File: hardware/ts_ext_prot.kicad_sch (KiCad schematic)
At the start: 4 parts

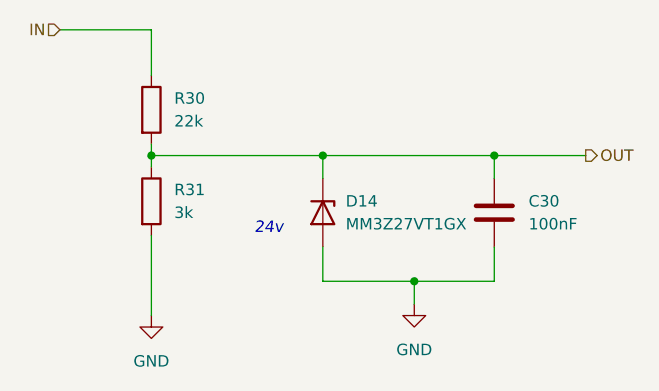
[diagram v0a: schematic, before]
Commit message: 0xERC State
Schematic needs only simulation and veryfying component choice for now
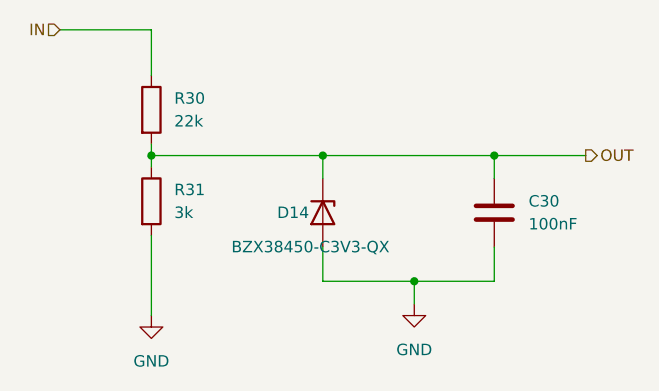
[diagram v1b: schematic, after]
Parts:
- D14: value MM3Z27VT1GX -> BZX38450-C3V3-QX; footprint Diode_SMD:D_SMB -> Diode_SMD:D_SOD-323_HandSoldering
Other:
- note removed: "24v"
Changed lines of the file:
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@@
     (stroke (width 0) (type default) (color 0 0 0 0))
-  )
-  (text "24v\n" (at 129.54 92.71 0)
-    (effects (font (size 1.27 1.27) italic) (justify left bottom))
   )
   (hierarchical_label "IN" (shape input) (at 107.95 69.85 180)
@@
   )
   (symbol (lib_id "Device:D_Zener") (at 137.16 90.17 270) (unit 1)
-    (in_bom yes) (on_board yes) (fields_autoplaced)
-    (property "Reference" "D14" (id 0) (at 139.7 88.8999 90)
+    (in_bom yes) (on_board yes)
+    (property "Reference" "D14" (id 0) (at 132.08 90.17 90)
       (effects (font (size 1.27 1.27)) (justify left))
     )
-    (property "Value" "MM3Z27VT1GX" (id 1) (at 139.7 91.4399 90)
+    (property "Value" "BZX38450-C3V3-QX" (id 1) (at 127 93.98 90)
       (effects (font (size 1.27 1.27)) (justify left))
     )
-    (property "Footprint" "Diode_SMD:D_SMB" (id 2) (at 137.16 90.17 0)
+    (property "Footprint" "Diode_SMD:D_SOD-323_HandSoldering" (id 2) (at 137.16 90.17 0)
       (effects (font (size 1.27 1.27)) hide)
     )
-    (property "Datasheet" "~" (id 3) (at 137.16 90.17 0)
+    (property "Datasheet" "https://www.mouser.pl/datasheet/2/916/BZX38450_Q_SER-2580608.pdf" (id 3) (at 137.16 90.17 0)
       (effects (font (size 1.27 1.27)) hide)
     )

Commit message: working simulations, assigned footprints
"nightly" relase
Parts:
- C30: value 100nF -> 10nF
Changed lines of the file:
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@@
       (effects (font (size 1.27 1.27)) (justify left))
     )
-    (property "Value" "100nF" (id 1) (at 160.02 91.4399 0)
+    (property "Value" "10nF" (id 1) (at 160.02 91.4399 0)
       (effects (font (size 1.27 1.27)) (justify left))
     )

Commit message: kończymy balet na dziś
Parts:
- R30, R31: footprint Resistor_SMD:R_0603_1608Metric -> Resistor_SMD:R_0603_1608Metric_Pad0.98x0.95mm_HandSolder
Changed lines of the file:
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@@
       (effects (font (size 1.27 1.27)) (justify left))
     )
-    (property "Footprint" "Resistor_SMD:R_0603_1608Metric" (id 2) (at 116.332 88.9 90)
+    (property "Footprint" "Resistor_SMD:R_0603_1608Metric_Pad0.98x0.95mm_HandSolder" (id 2) (at 116.332 88.9 90)
       (effects (font (size 1.27 1.27)) hide)
     )
@@
       (effects (font (size 1.27 1.27)) (justify left))
     )
-    (property "Footprint" "Resistor_SMD:R_0603_1608Metric" (id 2) (at 116.332 78.74 90)
+    (property "Footprint" "Resistor_SMD:R_0603_1608Metric_Pad0.98x0.95mm_HandSolder" (id 2) (at 116.332 78.74 90)
       (effects (font (size 1.27 1.27)) hide)
     )

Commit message: kurde no jeszcze nie skonczylem ale sune dalej
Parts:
- C30: footprint Capacitor_SMD:C_0201_0603Metric_Pad0.64x0.40mm_HandSolder -> Capacitor_SMD:C_0603_1608Metric_Pad1.08x0.95mm_HandSolder
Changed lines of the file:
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@@
       (effects (font (size 1.27 1.27)) (justify left))
     )
-    (property "Footprint" "Capacitor_SMD:C_0201_0603Metric_Pad0.64x0.40mm_HandSolder" (id 2) (at 157.1752 93.98 0)
+    (property "Footprint" "Capacitor_SMD:C_0603_1608Metric_Pad1.08x0.95mm_HandSolder" (id 2) (at 157.1752 93.98 0)
       (effects (font (size 1.27 1.27)) hide)
     )

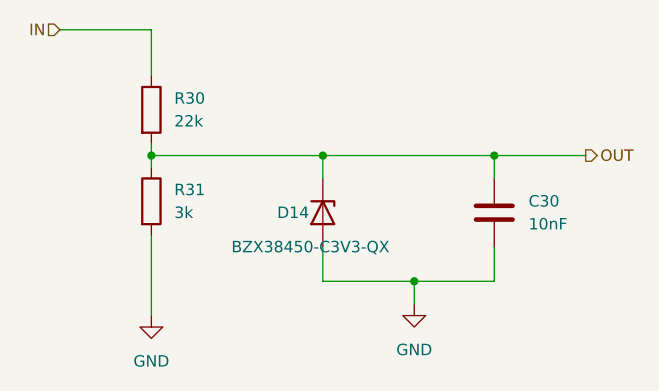
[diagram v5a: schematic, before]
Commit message: Schematic redesign for 23 rules, new pressure buffer, protection fix
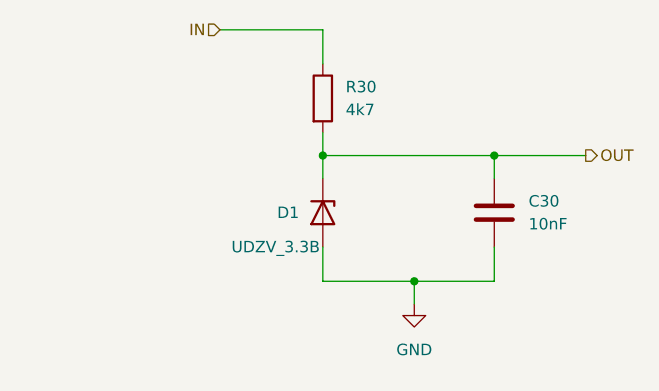
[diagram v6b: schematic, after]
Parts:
- removed D14: BZX38450-C3V3-QX, Diode_SMD:D_SOD-323_HandSoldering, symbol Device:D_Zener
- removed R31: 3k, Resistor_SMD:R_0603_1608Metric_Pad0.98x0.95mm_HandSolder, symbol Device:R
- added D1: UDZV_3.3B, Diode_SMD:D_SOD-323_HandSoldering, symbol Device:D_Zener
- R30: value 22k -> 4k7
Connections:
- net GND: now also D1.2 (A)
- net OUT: now also D1.1 (K)
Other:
- moved on the sheet: R30
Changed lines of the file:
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@@
   (junction (at 156.21 83.82) (diameter 0) (color 0 0 0 0)
-  )
-  (junction (at 118.11 83.82) (diameter 0) (color 0 0 0 0)
   )
   (junction (at 137.16 83.82) (diameter 0) (color 0 0 0 0)
@@
   (junction (at 147.32 97.79) (diameter 0) (color 0 0 0 0)
   )
-  (wire (pts (xy 107.95 69.85) (xy 118.11 69.85))
+  (wire (pts (xy 125.73 69.85) (xy 137.16 69.85))
     (stroke (width 0) (type default))
   )
-  (wire (pts (xy 118.11 82.55) (xy 118.11 83.82))
+  (wire (pts (xy 137.16 81.28) (xy 137.16 83.82))
     (stroke (width 0) (type default))
   )
   (wire (pts (xy 137.16 97.79) (xy 137.16 93.98))
-    (stroke (width 0) (type default))
-  )
-  (wire (pts (xy 118.11 83.82) (xy 118.11 85.09))
     (stroke (width 0) (type default))
   )
@@
     (stroke (width 0) (type default))
   )
-  (wire (pts (xy 118.11 74.93) (xy 118.11 69.85))
+  (wire (pts (xy 137.16 73.66) (xy 137.16 69.85))
     (stroke (width 0) (type default))
   )
@@
     (stroke (width 0) (type default))
   )
-  (wire (pts (xy 118.11 83.82) (xy 137.16 83.82))
-    (stroke (width 0) (type default))
-  )
-  (wire (pts (xy 118.11 92.71) (xy 118.11 101.6))
-    (stroke (width 0) (type default))
-  )
   (wire (pts (xy 147.32 100.33) (xy 147.32 97.79))
     (stroke (width 0) (type default))
@@
     (stroke (width 0) (type default))
   )
-  (hierarchical_label "IN" (shape input) (at 107.95 69.85 180) (fields_autoplaced)
+  (hierarchical_label "IN" (shape input) (at 125.73 69.85 180) (fields_autoplaced)
     (effects (font (size 1.27 1.27)) (justify right))
   )
@@
     (effects (font (size 1.27 1.27)) (justify left))
   )
-  (symbol (lib_id "Device:R") (at 118.11 88.9 0) (unit 1)
-    (in_bom yes) (on_board yes) (dnp no) (fields_autoplaced)
-    (property "Reference" "R31" (at 120.65 87.6299 0)
+  (symbol (lib_id "Device:D_Zener") (at 137.16 90.17 270) (unit 1)
+    (in_bom yes) (on_board yes) (dnp no)
+    (property "Reference" "D1" (at 132.08 90.17 90)
       (effects (font (size 1.27 1.27)) (justify left))
     )
-    (property "Value" "3k" (at 120.65 90.1699 0)
+    (property "Value" "UDZV_3.3B" (at 127 93.98 90)
       (effects (font (size 1.27 1.27)) (justify left))
     )
-    (property "Footprint" "Resistor_SMD:R_0603_1608Metric_Pad0.98x0.95mm_HandSolder" (at 116.332 88.9 90)
+    (property "Footprint" "Diode_SMD:D_SOD-323_HandSoldering" (at 137.16 90.17 0)
       (effects (font (size 1.27 1.27)) hide)
     )
-    (property "Datasheet" "~" (at 118.11 88.9 0)
+    (property "Datasheet" "https://www.mouser.pl/datasheet/2/916/BZX38450_Q_SER-2580608.pdf" (at 137.16 90.17 0)
       (effects (font (size 1.27 1.27)) hide)
     )
@@
     (instances
       (project "PUTM_DV_EBS_2023"
+        (path "/d921fbb5-521e-405d-bdec-f40195adfa1c/7da1b602-85c7-4e23-9ab2-6325d57b1abc"
+          (reference "D1") (unit 1)
+        )
+        (path "/d921fbb5-521e-405d-bdec-f40195adfa1c/7da1b602-85c7-4e23-9ab2-6325d57b1abc/6c904b20-f0d8-4a34-af03-c65fb29a5704"
+          (reference "D9") (unit 1)
+        )
         (path "/d921fbb5-521e-405d-bdec-f40195adfa1c/7da1b602-85c7-4e23-9ab2-6325d57b1abc/dae80125-d1c3-42fb-af9d-4a51941dd8ab"
-          (reference "R31") (unit 1)
+          (reference "D13") (unit 1)
         )
         (path "/d921fbb5-521e-405d-bdec-f40195adfa1c/7da1b602-85c7-4e23-9ab2-6325d57b1abc/7e3c265d-84b6-4eba-9091-794b8ba634be"
-          (reference "R33") (unit 1)
-        )
-        (path "/d921fbb5-521e-405d-bdec-f40195adfa1c/7da1b602-85c7-4e23-9ab2-6325d57b1abc/6c904b20-f0d8-4a34-af03-c65fb29a5704"
-          (reference "R29") (unit 1)
+          (reference "D14") (unit 1)
         )
       )
     )
   )
-  (symbol (lib_id "Device:R") (at 118.11 78.74 0) (unit 1)
+  (symbol (lib_id "Device:R") (at 137.16 77.47 0) (unit 1)
     (in_bom yes) (on_board yes) (dnp no) (fields_autoplaced)
-    (property "Reference" "R30" (at 120.65 77.4699 0)
+    (property "Reference" "R30" (at 139.7 76.1999 0)
       (effects (font (size 1.27 1.27)) (justify left))
     )
-    (property "Value" "22k" (at 120.65 80.0099 0)
+    (property "Value" "4k7" (at 139.7 78.7399 0)
       (effects (font (size 1.27 1.27)) (justify left))
     )
-    (property "Footprint" "Resistor_SMD:R_0603_1608Metric_Pad0.98x0.95mm_HandSolder" (at 116.332 78.74 90)
+    (property "Footprint" "Resistor_SMD:R_0603_1608Metric_Pad0.98x0.95mm_HandSolder" (at 135.382 77.47 90)
       (effects (font (size 1.27 1.27)) hide)
     )
-    (property "Datasheet" "~" (at 118.11 78.74 0)
+    (property "Datasheet" "~" (at 137.16 77.47 0)
       (effects (font (size 1.27 1.27)) hide)
     )
@@
     )
   )
-  (symbol (lib_id "Device:D_Zener") (at 137.16 90.17 270) (unit 1)
-    (in_bom yes) (on_board yes) (dnp no)
-    (property "Reference" "D14" (at 132.08 90.17 90)
-      (effects (font (size 1.27 1.27)) (justify left))
-    )
-    (property "Value" "BZX38450-C3V3-QX" (at 127 93.98 90)
-      (effects (font (size 1.27 1.27)) (justify left))
-    )
-    (property "Footprint" "Diode_SMD:D_SOD-323_HandSoldering" (at 137.16 90.17 0)
-      (effects (font (size 1.27 1.27)) hide)
-    )
-    (property "Datasheet" "https://www.mouser.pl/datasheet/2/916/BZX38450_Q_SER-2580608.pdf" (at 137.16 90.17 0)
-      (effects (font (size 1.27 1.27)) hide)
-    )
-    (pin "1")
-    (pin "2")
-    (instances
-      (project "PUTM_DV_EBS_2023"
-        (path "/d921fbb5-521e-405d-bdec-f40195adfa1c/7da1b602-85c7-4e23-9ab2-6325d57b1abc/dae80125-d1c3-42fb-af9d-4a51941dd8ab"
-          (reference "D14") (unit 1)
-        )
-        (path "/d921fbb5-521e-405d-bdec-f40195adfa1c/7da1b602-85c7-4e23-9ab2-6325d57b1abc/7e3c265d-84b6-4eba-9091-794b8ba634be"
-          (reference "D15") (unit 1)
-        )
-        (path "/d921fbb5-521e-405d-bdec-f40195adfa1c/7da1b602-85c7-4e23-9ab2-6325d57b1abc/6c904b20-f0d8-4a34-af03-c65fb29a5704"
-          (reference "D13") (unit 1)
-        )
-      )
-    )
-  )
   (symbol (lib_id "power:GND") (at 147.32 100.33 0) (unit 1)
     (in_bom yes) (on_board yes) (dnp no) (fields_autoplaced)
@@
         )
       )
-    )
-  )
-  (symbol (lib_id "power:GND") (at 118.11 101.6 0) (unit 1)
-    (in_bom yes) (on_board yes) (dnp no) (fields_autoplaced)
-    (property "Reference" "#PWR052" (at 118.11 107.95 0)
-      (effects (font (size 1.27 1.27)) hide)
-    )
-    (property "Value" "GND" (at 118.11 106.68 0)
-      (effects (font (size 1.27 1.27)))
-    )
-    (property "Footprint" "" (at 118.11 101.6 0)
-      (effects (font (size 1.27 1.27)) hide)
-    )
-    (property "Datasheet" "" (at 118.11 101.6 0)
-      (effects (font (size 1.27 1.27)) hide)
-    )
-    (pin "1")
-    (instances
-      (project "PUTM_DV_EBS_2023"
-        (path "/d921fbb5-521e-405d-bdec-f40195adfa1c/7da1b602-85c7-4e23-9ab2-6325d57b1abc/dae80125-d1c3-42fb-af9d-4a51941dd8ab"
-          (reference "#PWR052") (unit 1)
-        )
-        (path "/d921fbb5-521e-405d-bdec-f40195adfa1c/7da1b602-85c7-4e23-9ab2-6325d57b1abc/7e3c265d-84b6-4eba-9091-794b8ba634be"
-          (reference "#PWR054") (unit 1)
-        )
-        (path "/d921fbb5-521e-405d-bdec-f40195adfa1c/7da1b602-85c7-4e23-9ab2-6325d57b1abc/6c904b20-f0d8-4a34-af03-c65fb29a5704"
-          (reference "#PWR050") (unit 1)
-        )
-      )

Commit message: changed pcb version
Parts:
- removed D1: UDZV_3.3B, Diode_SMD:D_SOD-323_HandSoldering, symbol Device:D_Zener
- added D14: BZX38450-C3V3-QX, Diode_SMD:D_SOD-323_HandSoldering, symbol Device:D_Zener
- added R31: 3k, Resistor_SMD:R_0603_1608Metric_Pad0.98x0.95mm_HandSolder, symbol Device:R
- R30: value 4k7 -> 22k
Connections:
- net GND: now also D14.2 (A), R31.2
- net OUT: now also D14.1 (K), R31.1
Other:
- moved on the sheet: R30

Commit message: uploaded older pcb version
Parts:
- renumbered C30 to C29, D14 to D13, R30 to R28, R31 to R29
